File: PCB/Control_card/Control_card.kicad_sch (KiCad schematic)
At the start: 27 parts, among them IC1 TLSR8253F512ET48, J1 Conn_02x04_Counter_Clockwise, Y1 Crystal_GND24

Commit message: Ajout crystal
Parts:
- added D1, D2, D3, D4, D5: LED, symbol Device:LED
- added R1, R2, R3, R4, R5: R, symbol Device:R
- U1: footprint (none) -> Touch_Switch_Custom:BK7231N
- Y1: footprint (none) -> Touch_Switch_Custom:Crystal
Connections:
- net Relay1 is gone; now on net CT1: U1.8 (P8)
- net Relay2 is gone; now on net CT2: U1.9 (P7)
- net Relay3 is gone; now on net CT3: U1.10 (P6)
- net Relay4 is gone; now on net CT4: U1.11 (P26)
- net GND: now also D1.1 (K), D2.1 (K), D3.1 (K), D4.1 (K), D5.1 (K)
- net In1: now also IC1.2 (PA0)
- net In2: now also IC1.3 (PA1)
- net In3: now also IC1.4 (PA2)
- net In4: now also IC1.5 (PA3)
- net Net STT: now also R5.1
- net OutLed1: now also R1.1
- net OutLed2: now also R2.1
- net OutLed3: now also R3.1
- net OutLed4: now also R4.1
- net at L2.1: now also IC1.17 (VDCDC); no longer IC1.16 (VDCDC_SW)
- net at L2.2: now also IC1.16 (VDCDC_SW); no longer IC1.17 (VDCDC)
- new net: D2.2 (A), R2.2
- new net: D4.2 (A), R4.2
- new net: D1.2 (A), R1.2
- new net: D3.2 (A), R3.2
- new net: D5.2 (A), R5.2
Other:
- note added: "Control card for touch circuit"
- note added: "LEDs"
- note added: "May-June 2024"
- moved on the sheet: L2

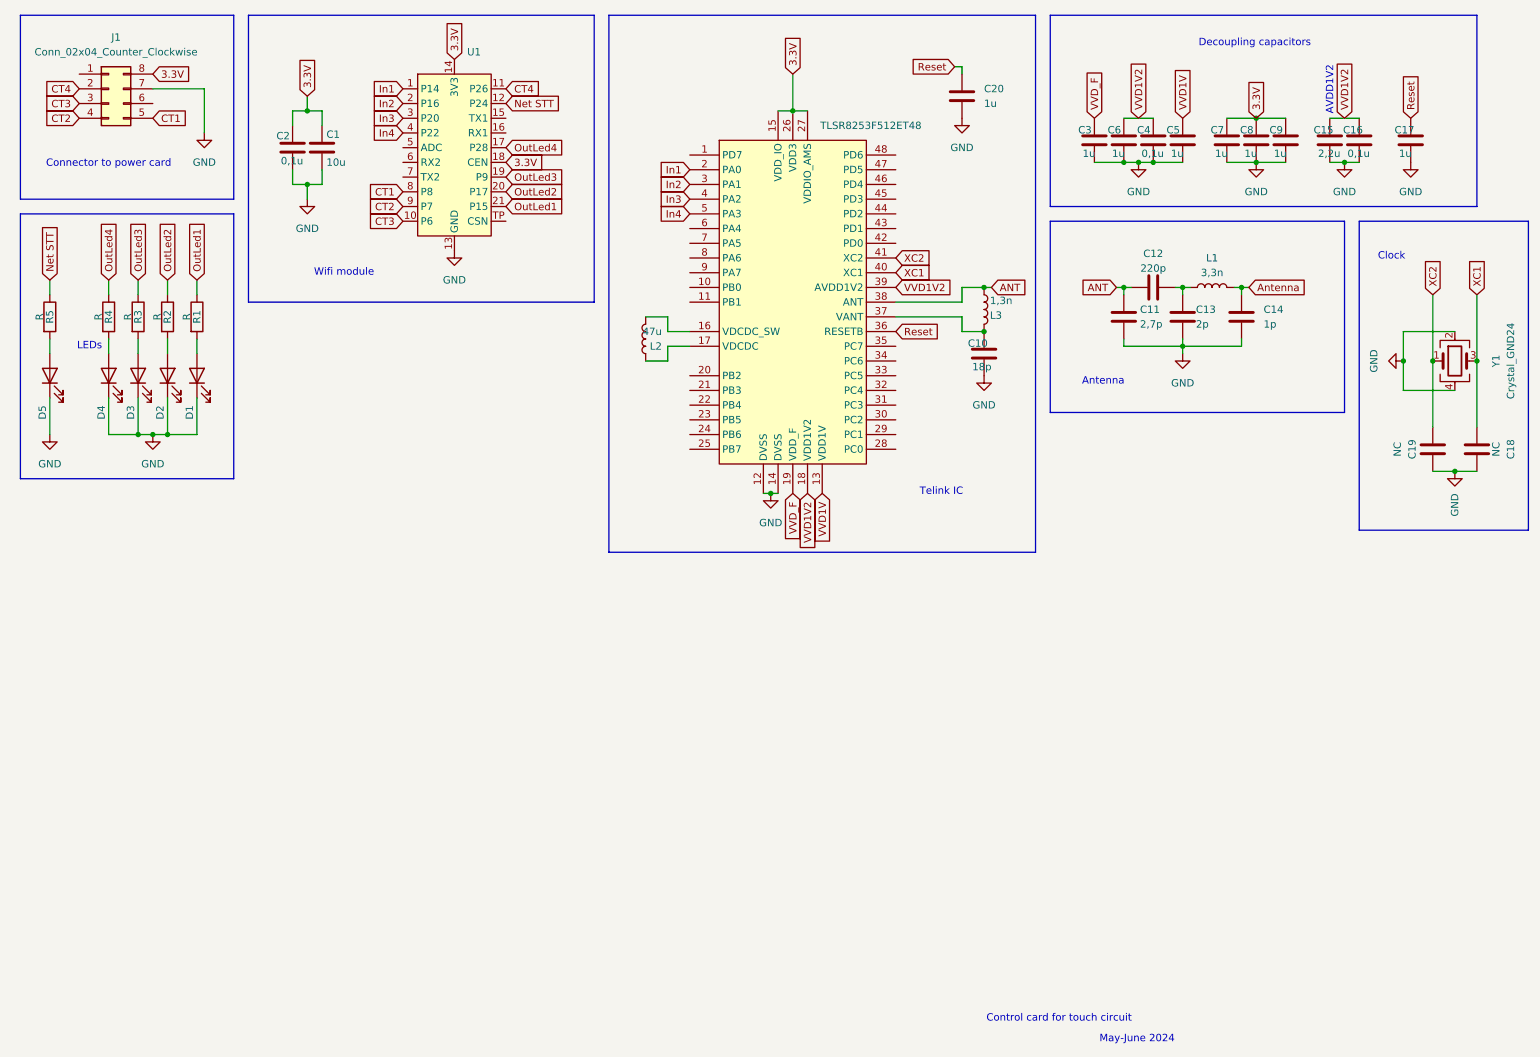
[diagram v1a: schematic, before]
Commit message: Continuation routage & ajout antenne
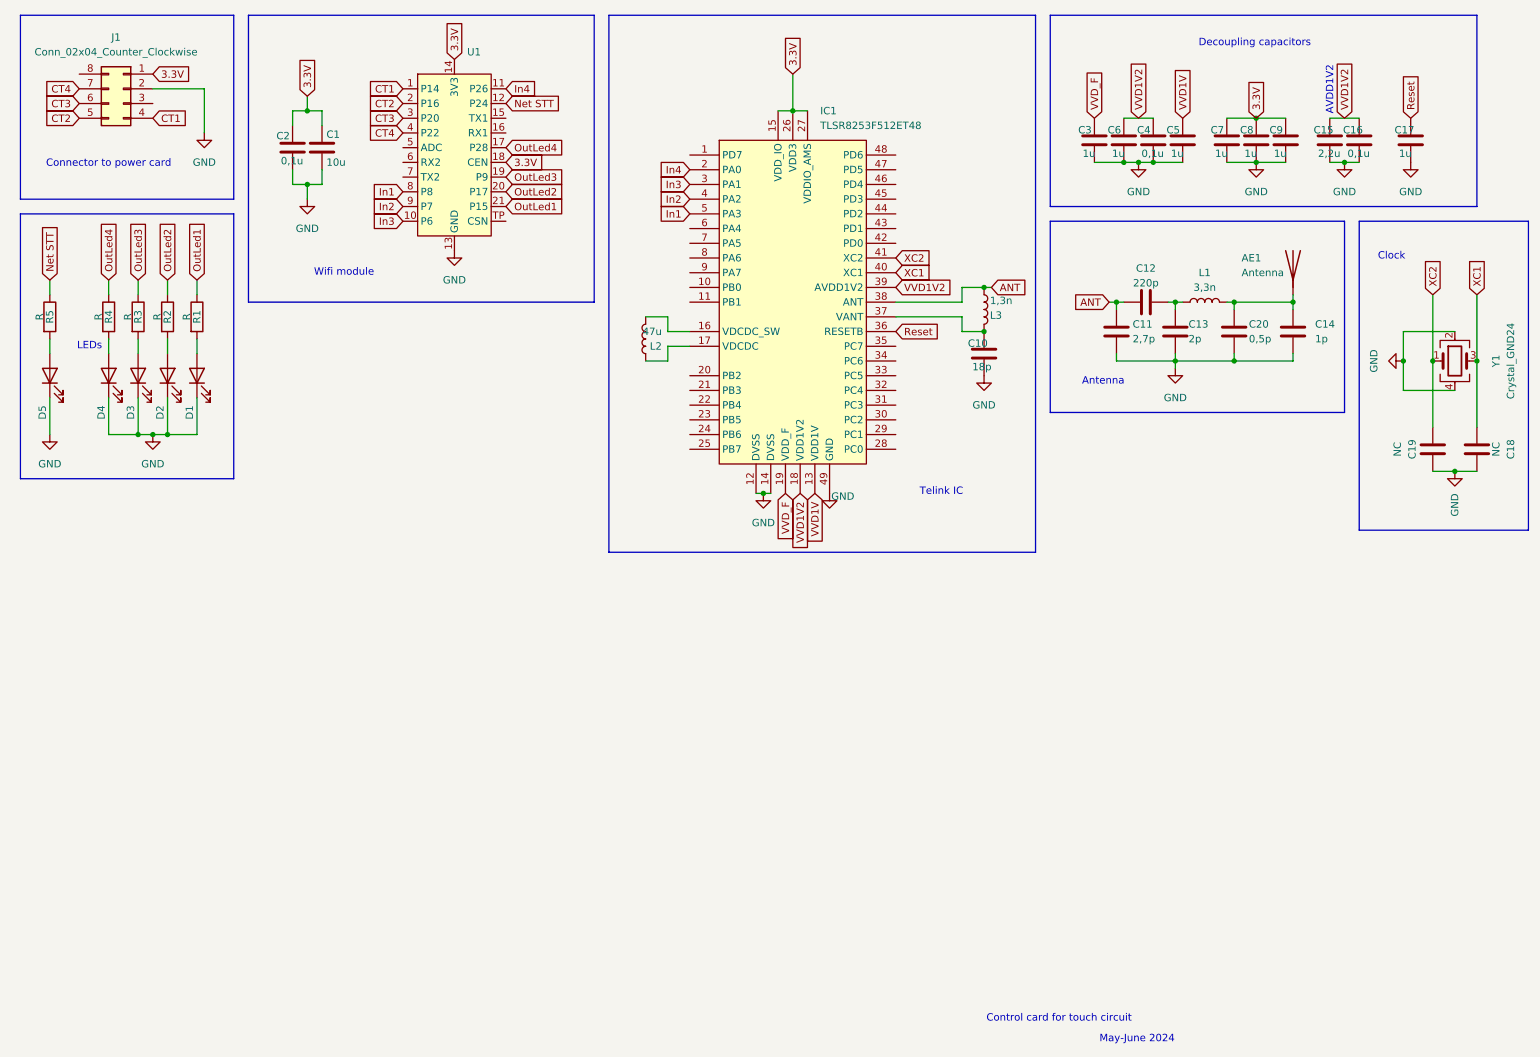
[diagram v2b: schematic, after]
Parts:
- added AE1: Antenna, Touch_Switch_Custom:Antenna, symbol Device:Antenna
- C1, C2: footprint (none) -> Capacitor_SMD:C_0402_1005Metric
- C20: value 1u -> 0,5p
- D1, D2, D3, D4, D5: footprint (none) -> LED_SMD:LED_0603_1608Metric
- R1, R2, R3, R4, R5: footprint (none) -> Resistor_SMD:R_0603_1608Metric
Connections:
- net 3.3V: now also J1.1 (Pin_1); no longer J1.8 (Pin_8)
- net CT1: now also J1.4 (Pin_4), U1.1 (P14); no longer J1.5 (Pin_5), U1.8 (P8)
- net CT2: now also J1.5 (Pin_5), U1.2 (P16); no longer J1.4 (Pin_4), U1.9 (P7)
- net CT3: now also J1.6 (Pin_6), U1.3 (P20); no longer J1.3 (Pin_3), U1.10 (P6)
- net CT4: now also J1.7 (Pin_7), U1.4 (P22); no longer J1.2 (Pin_2), U1.11 (P26)
- net GND: now also IC1.49 (GND), J1.2 (Pin_2); no longer J1.7 (Pin_7)
- net In1: now also IC1.5 (PA3), U1.8 (P8); no longer IC1.2 (PA0), U1.1 (P14)
- net In2: now also IC1.4 (PA2), U1.9 (P7); no longer IC1.3 (PA1), U1.2 (P16)
- net In3: now also IC1.3 (PA1), U1.10 (P6); no longer IC1.4 (PA2), U1.3 (P20)
- net In4: now also IC1.2 (PA0), U1.11 (P26); no longer IC1.5 (PA3), U1.4 (P22)
- net Reset: no longer C20.1
- net Antenna: no longer names the net of C14.1, L1.2
- net Antenna: now also C20.1, AE1.1 (A)
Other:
- moved on the sheet: C11, C12, C13, C14, L1

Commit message: Routage
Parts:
- removed AE1: Antenna, Touch_Switch_Custom:Antenna, symbol Device:Antenna
- added AE1: Antenna_Shield, Touch_Switch_Custom:Antenna, symbol Device:Antenna_Shield
- D1, D2, D3, D4, D5: footprint LED_SMD:LED_0603_1608Metric -> LED_SMD:LED_0805_2012Metric
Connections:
- net CT1: now also U1.8 (P8); no longer U1.1 (P14)
- net CT2: now also U1.9 (P7); no longer U1.2 (P16)
- net CT3: now also U1.10 (P6); no longer U1.3 (P20)
- net CT4: now also U1.11 (P26); no longer U1.4 (P22)
- net GND: now also AE1.2 (Shield)
- net In1: now also U1.1 (P14); no longer U1.8 (P8)
- net In2: now also U1.2 (P16); no longer U1.9 (P7)
- net In3: now also U1.3 (P20); no longer U1.10 (P6)
- net In4: now also U1.4 (P22); no longer U1.11 (P26)
- net at C14.1, C20.1, L1.2: now also AE1.1 (A)

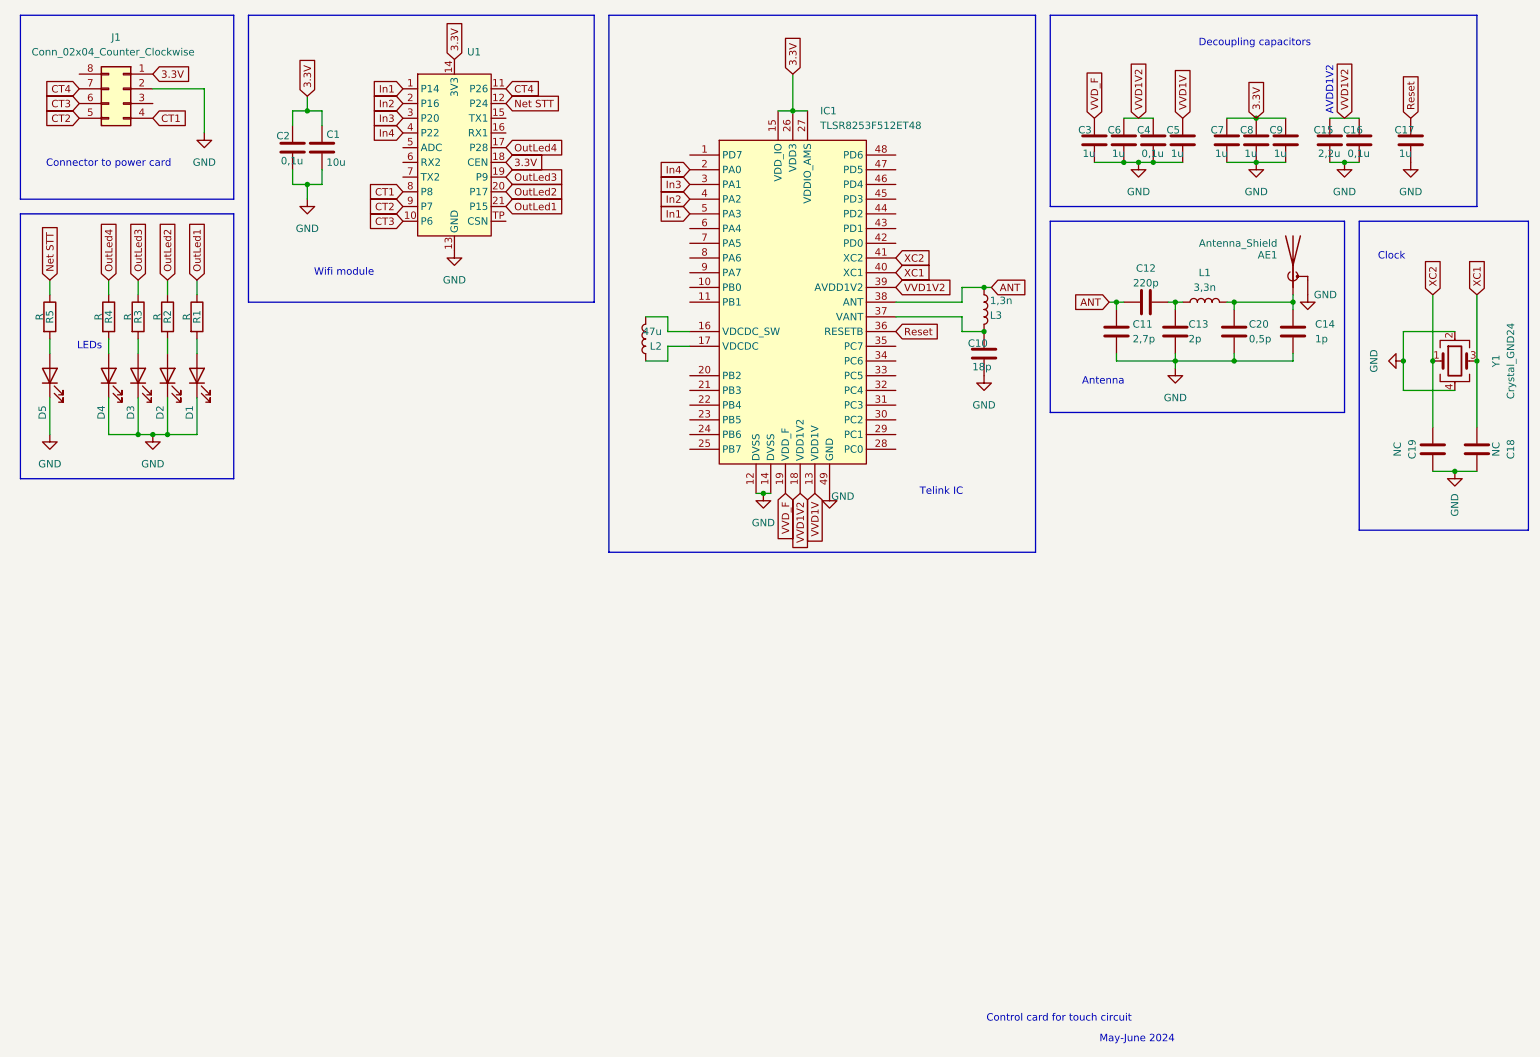
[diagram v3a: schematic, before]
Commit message: Ajout des touch switch
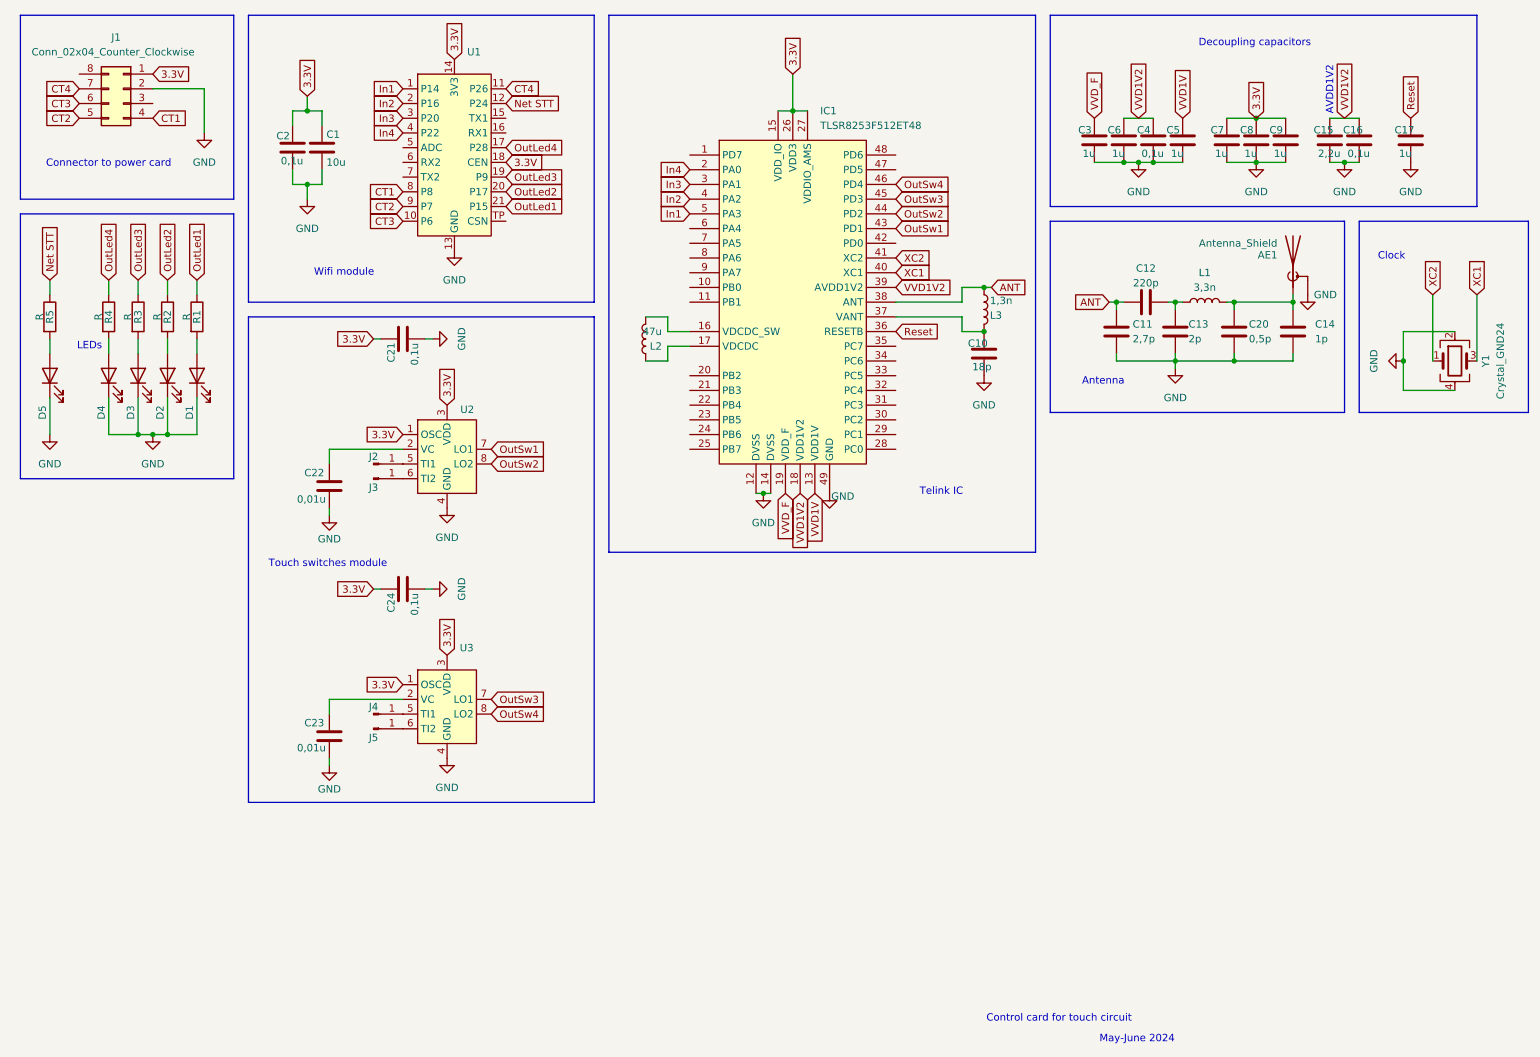
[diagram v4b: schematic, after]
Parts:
- removed C18, C19: NC, Capacitor_SMD:C_0402_1005Metric, symbol Device:C
- added C21, C24: 0,1u, Capacitor_SMD:C_0402_1005Metric, symbol Device:C
- added C22, C23: 0,01u, Capacitor_SMD:C_0402_1005Metric, symbol Device:C
- added J2, J3, J4, J5: Conn_01x01_Pin, Touch_Switch_Custom:Touch Switch, symbol Connector:Conn_01x01_Pin
- added U2, U3: ~, Package_SO:SOP-8_3.9x4.9mm_P1.27mm, symbol Touch_Switch_Custom:SGL8022K
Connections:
- net 3.3V: now also C21.1, C24.1, U2.1 (OSC), U2.3 (VDD), U3.1 (OSC), U3.3 (VDD)
- net GND: now also C21.2, C22.2, C23.2, C24.2, U2.4 (GND), U3.4 (GND)
- net OutSw1: now reaches IC1.43 (PD1)
- net OutSw1: now also U2.7 (LO1)
- net OutSw2: now reaches IC1.44 (PD2)
- net OutSw2: now also U2.8 (LO2)
- net OutSw3: now reaches IC1.45 (PD3)
- net OutSw3: now also U3.7 (LO1)
- net OutSw4: now reaches IC1.46 (PD4)
- net OutSw4: now also U3.8 (LO2)
- new net: C22.1, U2.2 (VC)
- new net: J2.1 (Pin_1), U2.5 (TI1)
- new net: J3.1 (Pin_1), U2.6 (TI2)
- new net: J5.1 (Pin_1), U3.6 (TI2)
- new net: J4.1 (Pin_1), U3.5 (TI1)
- new net: C23.1, U3.2 (VC)
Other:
- note added: "Touch switches module"

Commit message: Routage
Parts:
- J2, J3, J4, J5: footprint Touch_Switch_Custom:Touch Switch -> Touch_Switch_Custom:TouchSwitch
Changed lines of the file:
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@@
 			)
 		)
-		(property "Footprint" "Touch_Switch_Custom:Touch Switch"
+		(property "Footprint" "Touch_Switch_Custom:TouchSwitch"
 			(at 82.55 139.7 0)
 			(effects
@@
 			)
 		)
-		(property "Footprint" "Touch_Switch_Custom:Touch Switch"
+		(property "Footprint" "Touch_Switch_Custom:TouchSwitch"
 			(at 82.55 137.16 0)
 			(effects
@@
 			)
 		)
-		(property "Footprint" "Touch_Switch_Custom:Touch Switch"
+		(property "Footprint" "Touch_Switch_Custom:TouchSwitch"
 			(at 82.55 93.98 0)
 			(effects
@@
 			)
 		)
-		(property "Footprint" "Touch_Switch_Custom:Touch Switch"
+		(property "Footprint" "Touch_Switch_Custom:TouchSwitch"
 			(at 82.55 96.52 0)
 			(effects

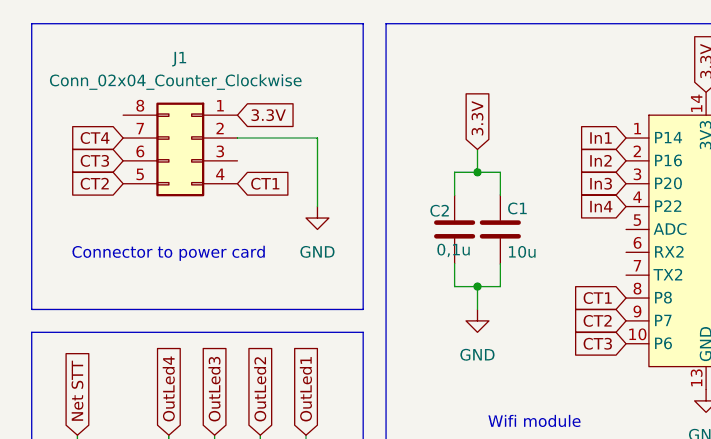
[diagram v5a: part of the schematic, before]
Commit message: Changement de connecteurs
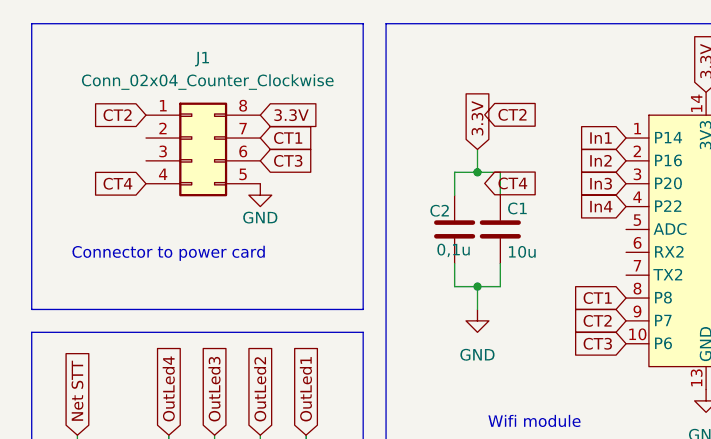
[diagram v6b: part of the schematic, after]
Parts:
- C1, C10, C11, C12, C13, C14, C15, C16, C17, C2, C20, C21, C22, C23, C24, C3, C4, C5, C6, C7, C8, C9: footprint Capacitor_SMD:C_0402_1005Metric -> Capacitor_SMD:C_0603_1608Metric
- J1: footprint Connector_PinHeader_2.54mm:PinHeader_2x04_P2.54mm_Vertical -> Touch_Switch_Custom:Pin mâle
- L1, L3: footprint Inductor_SMD:L_0402_1005Metric -> Inductor_SMD:L_0603_1608Metric
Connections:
- net 3.3V: now also J1.8 (Pin_8); no longer J1.1 (Pin_1)
- net CT1: now also J1.7 (Pin_7); no longer J1.4 (Pin_4)
- net CT2: now also J1.1 (Pin_1); no longer J1.5 (Pin_5)
- net CT4: now also J1.4 (Pin_4); no longer J1.7 (Pin_7)
- net GND: now also J1.5 (Pin_5); no longer J1.2 (Pin_2)
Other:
- moved on the sheet: J1

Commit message: Ajout des footprints
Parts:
- J1: footprint Touch_Switch_Custom:Pin mâle -> Touch_Switch_Custom:PinMale
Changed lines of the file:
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@@
 			)
 		)
-		(property "Footprint" "Touch_Switch_Custom:Pin mâle"
+		(property "Footprint" "Touch_Switch_Custom:PinMale"
 			(at 39.37 29.21 0)
 			(effects

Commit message: Rota IC contrôle
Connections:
- net OutSw1: now also IC1.46 (PD4); no longer IC1.43 (PD1)
- net OutSw2: now also IC1.45 (PD3); no longer IC1.44 (PD2)
- net OutSw3: now also IC1.44 (PD2); no longer IC1.45 (PD3)
- net OutSw4: now also IC1.43 (PD1); no longer IC1.46 (PD4)
